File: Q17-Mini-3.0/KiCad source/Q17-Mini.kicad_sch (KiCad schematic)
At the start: 82 parts, among them J1 INPUT, J2-1 SPK+, J2-2 SPK-, J3-1 V+, J3-2 GND, J3-3 V-, Q1 IRF610, Q10 KSA992, Q12 KSC1845, Q13 IRF610, Q14 IRF9610, Q15 FQA46N15, Q16 IXTQ36P15P, Q2 KSA992, Q3 KSC1845, Q4 IRF9610, Q5 FQPF7P20, Q6 2SK3564, Q7 LSK170B, Q8 DN2540, Q9 BS250P, U1 OPA1611, U2 NDC7003P

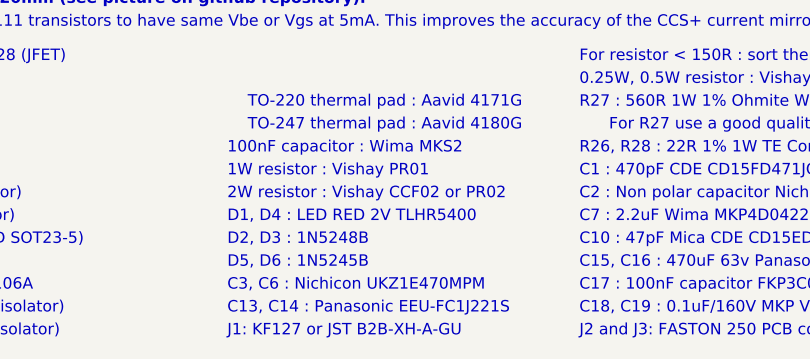
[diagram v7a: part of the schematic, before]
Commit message: Update Q17-Mini diagram
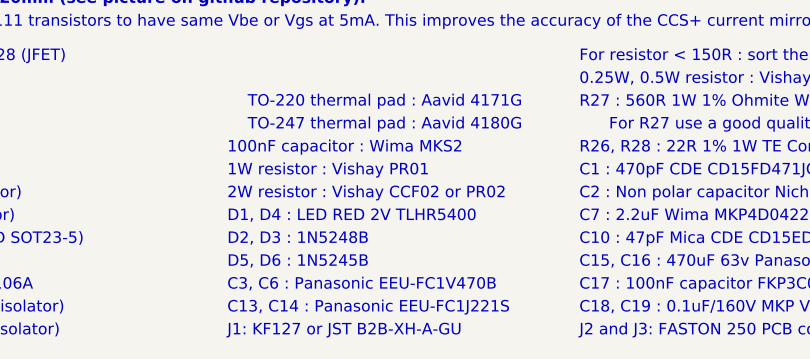
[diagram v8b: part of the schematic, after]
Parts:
- C3, C6: Mouser 647-UKW2A470MPD -> 667-EEU-FC1V470B; Part# UKW2A470MPD -> EEU-FC1V470B
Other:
- note added: "C3, C6 : Panasonic EEU-FC1V470B"
- note removed: "C3, C6 : Nichicon UKZ1E470MPM"
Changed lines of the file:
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@@
 	(title_block
 		(title "Q17-Mini Amplifier")
-		(date "2024-08-26")
-		(rev "2.3.4")
+		(date "2024-08-31")
+		(rev "2.3.5")
 		(company "Principe circuit by Tiberiu Vicol")
 		(comment 1 "Modified by Stef for the Q17-Mini project")
@@
 		)
 	)
-	(text "C3, C6 : Nichicon UKZ1E470MPM"
+	(text "C3, C6 : Panasonic EEU-FC1V470B"
 		(exclude_from_sim no)
 		(at 68.834 191.77 0)
@@
 			)
 		)
-		(property "Datasheet" "https://www.mouser.fr/datasheet/2/293/e_ukw-1919118.pdf"
+		(property "Datasheet" "https://www.mouser.fr/datasheet/2/315/ABA0000C1209-1289053.pdf"
 			(at 63.5 107.95 0)
 			(effects
@@
 			)
 		)
-		(property "Part#" "UKW2A470MPD"
+		(property "Part#" "EEU-FC1V470B"
 			(at 63.5 107.95 90)
 			(effects
@@
 			)
 		)
-		(property "Mouser" "647-UKW2A470MPD"
+		(property "Mouser" "667-EEU-FC1V470B"
 			(at 63.5 107.95 90)
 			(effects
@@
 			)
 		)
-		(property "Datasheet" "https://www.mouser.fr/datasheet/2/293/e_ukw-1919118.pdf"
+		(property "Datasheet" "https://www.mouser.fr/datasheet/2/315/ABA0000C1209-1289053.pdf"
 			(at 63.5 57.15 0)
 			(effects
@@
 			)
 		)
-		(property "Part#" "UKW2A470MPD"
+		(property "Part#" "EEU-FC1V470B"
 			(at 63.5 57.15 90)
 			(effects
@@
 			)
 		)
-		(property "Mouser" "647-UKW2A470MPD"
+		(property "Mouser" "667-EEU-FC1V470B"
 			(at 63.5 57.15 90)
 			(effects
